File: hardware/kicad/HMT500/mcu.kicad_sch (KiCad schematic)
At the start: 7 parts, among them J2 TC2030-IDC-NL, U4 STM32G0B1CCT3

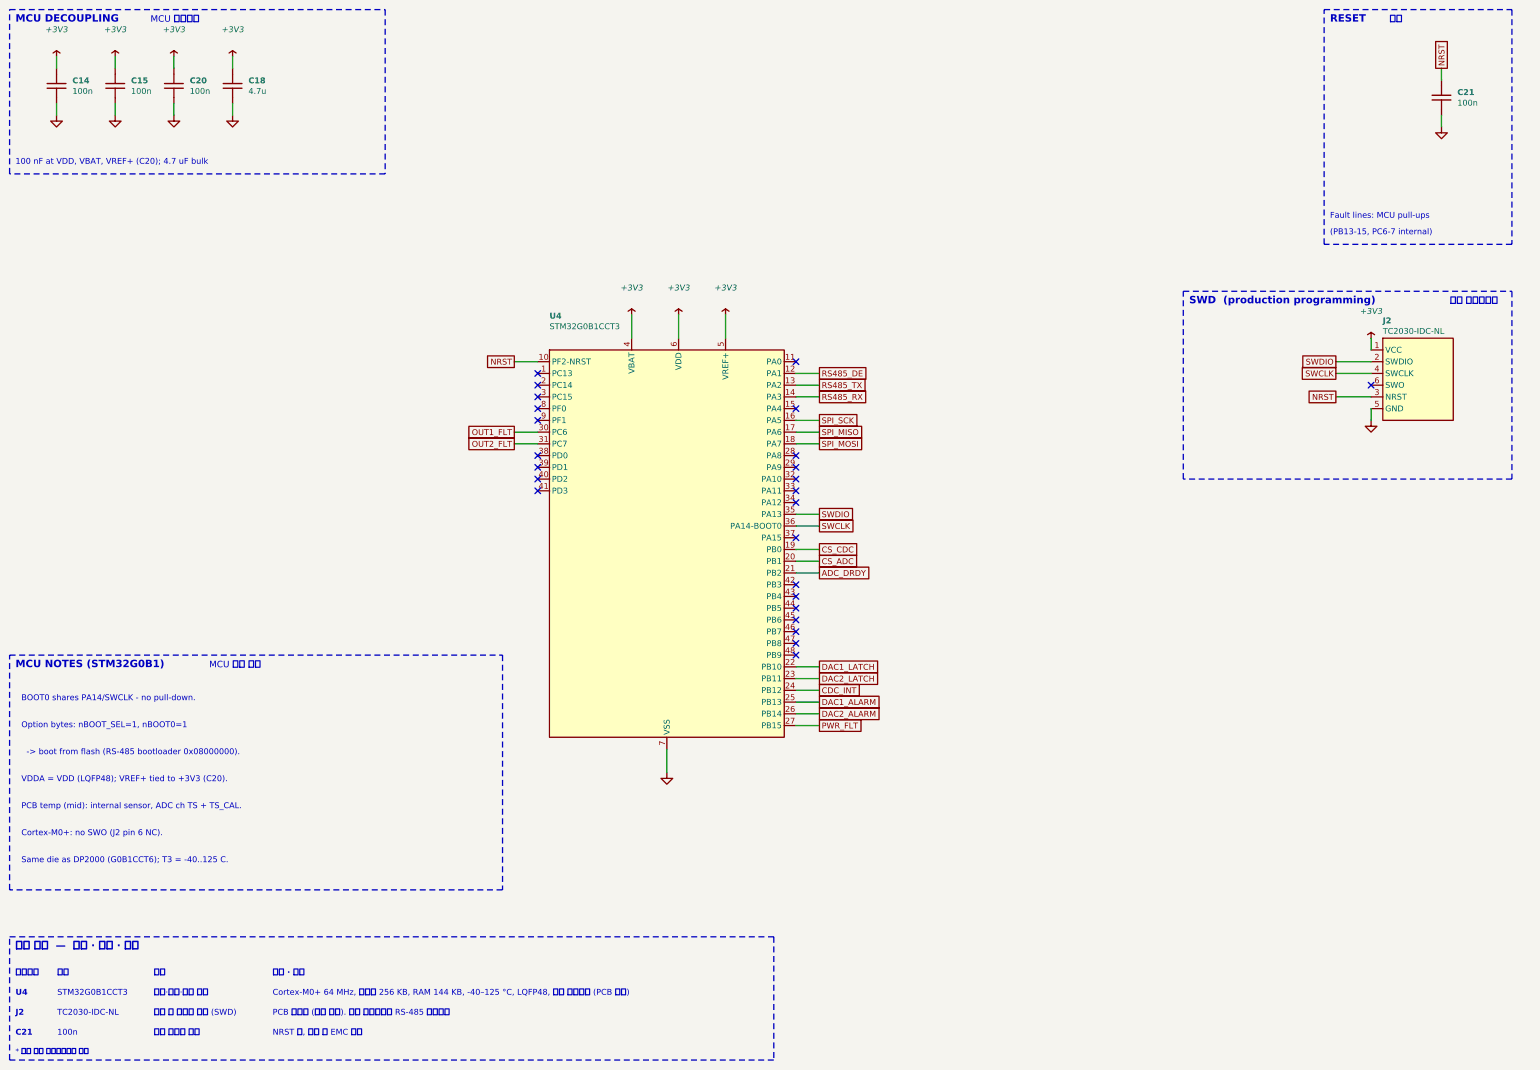
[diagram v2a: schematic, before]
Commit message: Schematic v0.7: DAC8760 real pinout, OPA197 +VSENSE buffer, ISET-R, SPI2 daisy chain
- DAC8760 symbol from datasheet SBAS528D (HTSSOP-24 PWP + EP), same as
  VibrationSensor IVS320; placeholder pins removed, VERIFY flag dropped
- +VSENSE via OPA197 unity-gain follower (U12/U13) of the terminal voltage;
  R31/R41 10k kept as buffer input protection; C45/C55 V+ bypass
- External ISET-R 15k 0.1% 25 ppm (R32/R42)
- DACs on dedicated SPI2 (PB13/14/15) daisy chain with common DAC_LATCH
  (PB10); R33 100k pull-down on DAC_DAISY; ALARM -> PB11/PB3, PWR_FLT -> PB4
- Output protection unification (TPS26611 vs passive) left on hold
- Parts list, circuit-design doc, decision log #24 updated; netlist 70/70, 0 errors

Co-Authored-By: Claude Opus 5.5 <noreply@anthropic.com>
Claude-Session: https://claude.ai/code/session_01JA2o8uJsqp9Vzsg4b665ev
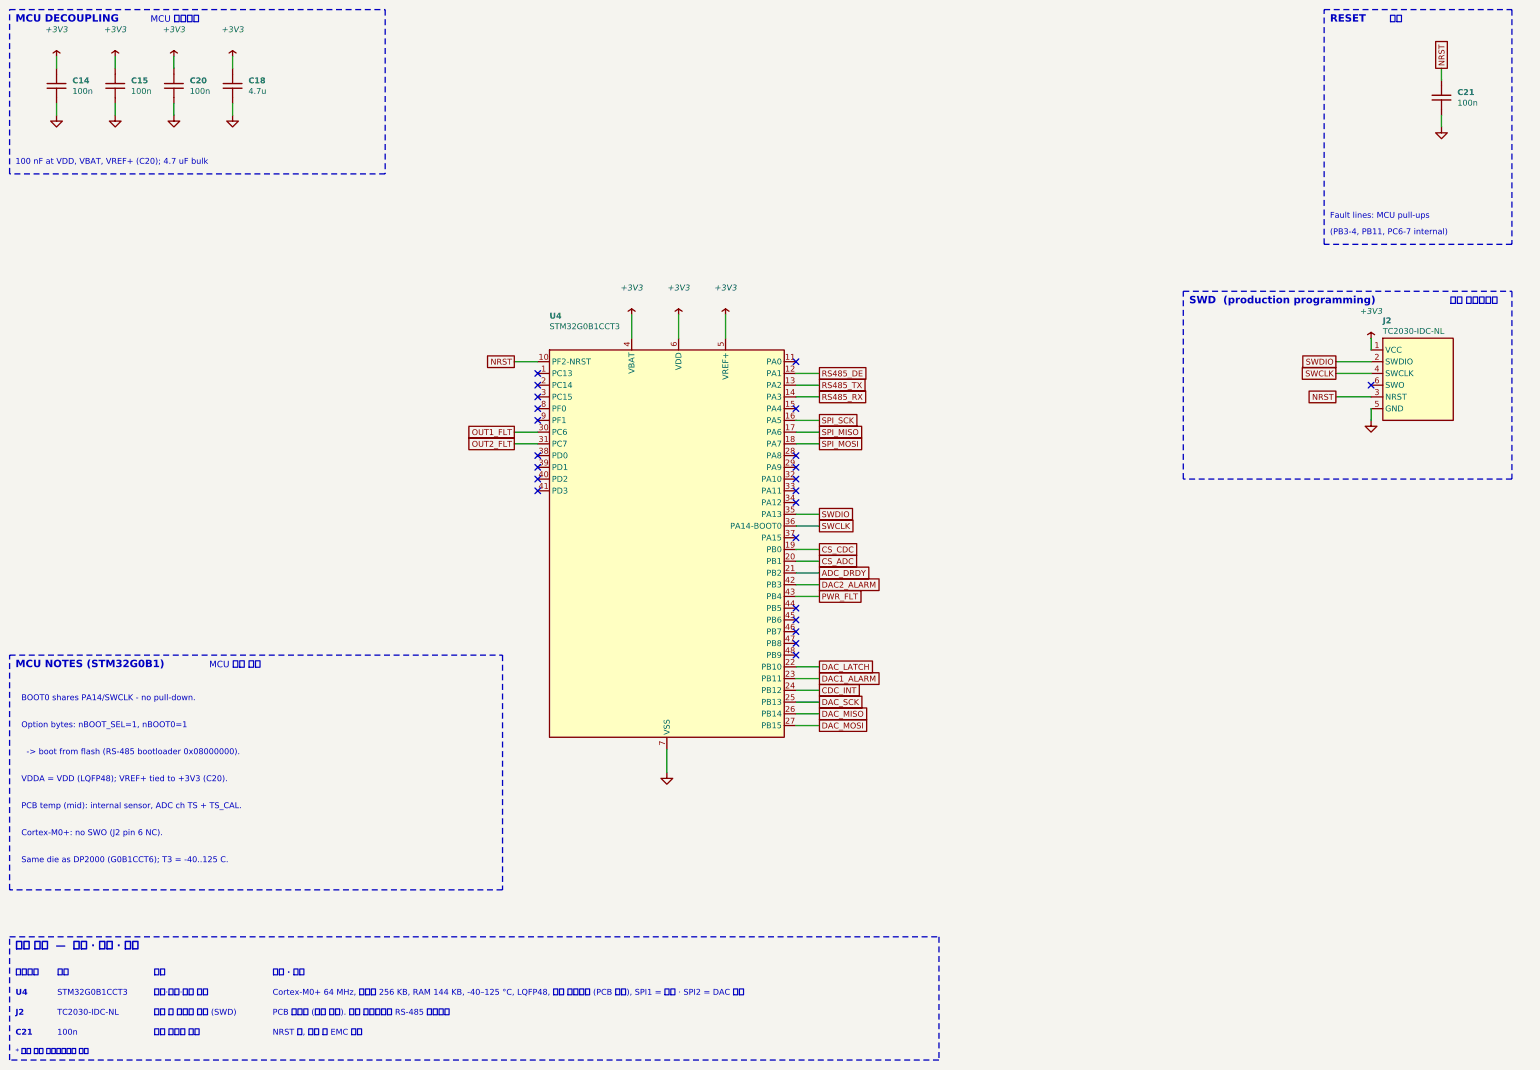
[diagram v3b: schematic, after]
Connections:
- net DAC2_LATCH is gone; now on net DAC1_ALARM: U4.23 (PB11)
- net DAC1_ALARM: no longer U4.25 (PB13)
- net DAC2_ALARM: now also U4.42 (PB3); no longer U4.26 (PB14)
- net PWR_FLT: now also U4.43 (PB4); no longer U4.27 (PB15)
- net DAC1_LATCH renamed DAC_LATCH
- new net DAC_MISO: U4.26 (PB14)
- new net DAC_MOSI: U4.27 (PB15)
- new net DAC_SCK: U4.25 (PB13)
- no-connect marks 25 -> 23
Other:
- note added: "(PB3-4, PB11, PC6-7 internal)"
- note added: "Cortex-M0+ 64 MHz, 플래시 256 KB, RAM 144 KB, -40–125 °C, LQFP48, 내부 온도센서 (PCB 온도), SPI1 = 측정 · SPI2 = DAC 전용"
- note removed: "(PB13-15, PC6-7 internal)"
- note removed: "Cortex-M0+ 64 MHz, 플래시 256 KB, RAM 144 KB, -40–125 °C, LQFP48, 내부 온도센서 (PCB 온도)"
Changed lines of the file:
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@@
 (kicad_sch (version 20230121) (generator eeschema) (paper "A3")
-(title_block (title "HMT500  MCU") (date "2026-09-29") (rev "0.6") (company "DOTECH Co., Ltd.") (comment 1 "Oil moisture transmitter HMT500 - RS-485 + 2x V/I analog output") (comment 2 "Design notes: docs/hw/circuit-design.md") (comment 3 "VERIFY=YES parts: pin numbers LMR36006/PCAP04/DAC8760/TPS26611; TPS2660 R22"))
+(title_block (title "HMT500  MCU") (date "2026-09-29") (rev "0.7") (company "DOTECH Co., Ltd.") (comment 1 "Oil moisture transmitter HMT500 - RS-485 + 2x V/I analog output") (comment 2 "Design notes: docs/hw/circuit-design.md") (comment 3 "VERIFY=YES parts: pin numbers LMR36006/PCAP04/TPS26611; TPS2660 R22"))
 (symbol (lib_id "HMT500:STM32G0B1CxTx") (at 172.72 147.32 0) (unit 1) (in_bom yes) (on_board yes) (dnp no) (property "Reference" "U4" (at 147.32 99.314 0) (effects (font (size 1.27 1.27) bold) (justify left))) (property "Value" "STM32G0B1CCT3" (at 147.32 101.6 0) (effects (font (size 1.27 1.27)) (justify left))) (property "Footprint" "Package_QFP:LQFP-48_7x7mm_P0.5mm" (at 172.72 147.32 0) (effects (font (size 1.27 1.27)) hide)) (property "Datasheet" "~" (at 172.72 147.32 0) (effects (font (size 1.27 1.27)) hide)) (pin "10") (pin "1") (pin "2") (pin "3") (pin "8") (pin "9") (pin "30") (pin "31") (pin "38") (pin "39") (pin "40") (pin "41") (pin "11") (pin "12") (pin "13") (pin "14") (pin "15") (pin "16") (pin "17") (pin "18") (pin "28") (pin "29") (pin "32") (pin "33") (pin "34") (pin "35") (pin "36") (pin "37") (pin "19") (pin "20") (pin "21") (pin "42") (pin "43") (pin "44") (pin "45") (pin "46") (pin "47") (pin "48") (pin "22") (pin "23") (pin "24") (pin "25") (pin "26") (pin "27") (pin "4") (pin "6") (pin "5") (pin "7") (instances (project "HMT500" (path "/1ebb025b-11bd-5f7c-aaab-41e2a750e8b3/0c4bf7d4-9d5c-53b1-9acd-02d419e0823f" (reference "U4") (unit 1)))))
 (symbol (lib_id "HMT500:+3V3") (at 165.1 99.06 0) (unit 1) (in_bom no) (on_board no) (dnp no) (property "Reference" "#PWR043" (at 165.1 90.932 0) (effects (font (size 1.27 1.27) bold) hide)) (property "Value" "+3V3" (at 165.1 93.218 0) (effects (font (size 1.27 1.27) italic))) (property "Footprint" "" (at 165.1 99.06 0) (effects (font (size 1.27 1.27)) hide)) (property "Datasheet" "~" (at 165.1 99.06 0) (effects (font (size 1.27 1.27)) hide)) (pin "1") (instances (project "HMT500" (path "/1ebb025b-11bd-5f7c-aaab-41e2a750e8b3/0c4bf7d4-9d5c-53b1-9acd-02d419e0823f" (reference "#PWR043") (unit 1)))))
@@
 (wire (pts (xy 200.66 152.4) (xy 205.74 152.4)) (stroke (width 0) (type default)))
 (wire (pts (xy 200.66 154.94) (xy 205.74 154.94)) (stroke (width 0) (type default)))
+(wire (pts (xy 200.66 157.48) (xy 205.74 157.48)) (stroke (width 0) (type default)))
+(wire (pts (xy 200.66 160.02) (xy 205.74 160.02)) (stroke (width 0) (type default)))
 (wire (pts (xy 200.66 175.26) (xy 205.74 175.26)) (stroke (width 0) (type default)))
 (wire (pts (xy 200.66 177.8) (xy 205.74 177.8)) (stroke (width 0) (type default)))
@@
 (global_label "CS_ADC" (shape passive) (at 205.74 152.4 0) (fields_autoplaced) (effects (font (size 1.27 1.27)) (justify left)) (property "Intersheetrefs" "${INTERSHEET_REFS}" (at 205.74 152.4 0) (effects (font (size 1.27 1.27)) hide)))
 (global_label "ADC_DRDY" (shape passive) (at 205.74 154.94 0) (fields_autoplaced) (effects (font (size 1.27 1.27)) (justify left)) (property "Intersheetrefs" "${INTERSHEET_REFS}" (at 205.74 154.94 0) (effects (font (size 1.27 1.27)) hide)))
-(global_label "DAC1_LATCH" (shape passive) (at 205.74 175.26 0) (fields_autoplaced) (effects (font (size 1.27 1.27)) (justify left)) (property "Intersheetrefs" "${INTERSHEET_REFS}" (at 205.74 175.26 0) (effects (font (size 1.27 1.27)) hide)))
-(global_label "DAC2_LATCH" (shape passive) (at 205.74 177.8 0) (fields_autoplaced) (effects (font (size 1.27 1.27)) (justify left)) (property "Intersheetrefs" "${INTERSHEET_REFS}" (at 205.74 177.8 0) (effects (font (size 1.27 1.27)) hide)))
+(global_label "DAC2_ALARM" (shape passive) (at 205.74 157.48 0) (fields_autoplaced) (effects (font (size 1.27 1.27)) (justify left)) (property "Intersheetrefs" "${INTERSHEET_REFS}" (at 205.74 157.48 0) (effects (font (size 1.27 1.27)) hide)))
+(global_label "PWR_FLT" (shape passive) (at 205.74 160.02 0) (fields_autoplaced) (effects (font (size 1.27 1.27)) (justify left)) (property "Intersheetrefs" "${INTERSHEET_REFS}" (at 205.74 160.02 0) (effects (font (size 1.27 1.27)) hide)))
+(global_label "DAC_LATCH" (shape passive) (at 205.74 175.26 0) (fields_autoplaced) (effects (font (size 1.27 1.27)) (justify left)) (property "Intersheetrefs" "${INTERSHEET_REFS}" (at 205.74 175.26 0) (effects (font (size 1.27 1.27)) hide)))
+(global_label "DAC1_ALARM" (shape passive) (at 205.74 177.8 0) (fields_autoplaced) (effects (font (size 1.27 1.27)) (justify left)) (property "Intersheetrefs" "${INTERSHEET_REFS}" (at 205.74 177.8 0) (effects (font (size 1.27 1.27)) hide)))
 (global_label "CDC_INT" (shape passive) (at 205.74 180.34 0) (fields_autoplaced) (effects (font (size 1.27 1.27)) (justify left)) (property "Intersheetrefs" "${INTERSHEET_REFS}" (at 205.74 180.34 0) (effects (font (size 1.27 1.27)) hide)))
-(global_label "DAC1_ALARM" (shape passive) (at 205.74 182.88 0) (fields_autoplaced) (effects (font (size 1.27 1.27)) (justify left)) (property "Intersheetrefs" "${INTERSHEET_REFS}" (at 205.74 182.88 0) (effects (font (size 1.27 1.27)) hide)))
-(global_label "DAC2_ALARM" (shape passive) (at 205.74 185.42 0) (fields_autoplaced) (effects (font (size 1.27 1.27)) (justify left)) (property "Intersheetrefs" "${INTERSHEET_REFS}" (at 205.74 185.42 0) (effects (font (size 1.27 1.27)) hide)))
-(global_label "PWR_FLT" (shape passive) (at 205.74 187.96 0) (fields_autoplaced) (effects (font (size 1.27 1.27)) (justify left)) (property "Intersheetrefs" "${INTERSHEET_REFS}" (at 205.74 187.96 0) (effects (font (size 1.27 1.27)) hide)))
+(global_label "DAC_SCK" (shape passive) (at 205.74 182.88 0) (fields_autoplaced) (effects (font (size 1.27 1.27)) (justify left)) (property "Intersheetrefs" "${INTERSHEET_REFS}" (at 205.74 182.88 0) (effects (font (size 1.27 1.27)) hide)))
+(global_label "DAC_MISO" (shape passive) (at 205.74 185.42 0) (fields_autoplaced) (effects (font (size 1.27 1.27)) (justify left)) (property "Intersheetrefs" "${INTERSHEET_REFS}" (at 205.74 185.42 0) (effects (font (size 1.27 1.27)) hide)))
+(global_label "DAC_MOSI" (shape passive) (at 205.74 187.96 0) (fields_autoplaced) (effects (font (size 1.27 1.27)) (justify left)) (property "Intersheetrefs" "${INTERSHEET_REFS}" (at 205.74 187.96 0) (effects (font (size 1.27 1.27)) hide)))
 (global_label "NRST" (shape passive) (at 340.36 45.72 90) (fields_autoplaced) (effects (font (size 1.27 1.27)) (justify left)) (property "Intersheetrefs" "${INTERSHEET_REFS}" (at 340.36 45.72 0) (effects (font (size 1.27 1.27)) hide)))
 (global_label "SWDIO" (shape passive) (at 317.5 109.22 180) (fields_autoplaced) (effects (font (size 1.27 1.27)) (justify right)) (property "Intersheetrefs" "${INTERSHEET_REFS}" (at 317.5 109.22 0) (effects (font (size 1.27 1.27)) hide)))
@@
 (no_connect (at 200.66 139.7))
 (no_connect (at 200.66 147.32))
-(no_connect (at 200.66 157.48))
-(no_connect (at 200.66 160.02))
 (no_connect (at 200.66 162.56))
 (no_connect (at 200.66 165.1))
@@
 (rectangle (start 284.48 93.98) (end 355.6 134.62) (stroke (width 0.1524) (type dash) (color 72 72 160 1)) (fill (type none)))
 (rectangle (start 30.48 172.72) (end 137.16 223.52) (stroke (width 0.1524) (type dash) (color 72 72 160 1)) (fill (type none)))
-(rectangle (start 30.48 233.68) (end 195.859 260.35) (stroke (width 0.1524) (type dash) (color 72 72 160 1)) (fill (type none)))
+(rectangle (start 30.48 233.68) (end 231.61 260.35) (stroke (width 0.1524) (type dash) (color 72 72 160 1)) (fill (type none)))
 (text "MCU DECOUPLING" (at 31.75 36.068 0) (effects (font (size 1.6 1.6) bold) (justify left bottom)))
 (text "MCU 바이패스" (at 60.9616 36.068 0) (effects (font (face "NanumGothic") (size 1.4 1.4)) (justify left bottom)))
@@
 (text "리셋" (at 329.112 36.068 0) (effects (font (face "NanumGothic") (size 1.4 1.4)) (justify left bottom)))
 (text "Fault lines: MCU pull-ups" (at 316.23 78.486 0) (effects (font (size 1.27 1.27)) (justify left bottom)))
-(text "(PB13-15, PC6-7 internal)" (at 316.23 82.042 0) (effects (font (size 1.27 1.27)) (justify left bottom)))
+(text "(PB3-4, PB11, PC6-7 internal)" (at 316.23 82.042 0) (effects (font (size 1.27 1.27)) (justify left bottom)))
 (text "SWD  (production programming)" (at 285.75 97.028 0) (effects (font (size 1.6 1.6) bold) (justify left bottom)))
 (text "생산 프로그래밍" (at 342.178 97.028 0) (effects (font (face "NanumGothic") (size 1.4 1.4)) (justify left bottom)))
@@
 (text "STM32G0B1CCT3" (at 40.7924 246.634 0) (effects (font (size 1.27 1.27)) (justify left bottom)))
 (text "제어·통신·보정 연산" (at 61.6839 246.634 0) (effects (font (face "NanumGothic") (size 1.27 1.27)) (justify left bottom)))
-(text "Cortex-M0+ 64 MHz, 플래시 256 KB, RAM 144 KB, -40–125 °C, LQFP48, 내부 온도센서 (PCB 온도)" (at 87.4014 246.634 0) (effects (font (face "NanumGothic") (size 1.27 1.27)) (justify left bottom)))
+(text "Cortex-M0+ 64 MHz, 플래시 256 KB, RAM 144 KB, -40–125 °C, LQFP48, 내부 온도센서 (PCB 온도), SPI1 = 측정 · SPI2 = DAC 전용" (at 87.4014 246.634 0) (effects (font (face "NanumGothic") (size 1.27 1.27)) (justify left bottom)))
 (text "J2" (at 31.75 250.952 0) (effects (font (size 1.27 1.27) bold) (justify left bottom)))
 (text "TC2030-IDC-NL" (at 40.7924 250.952 0) (effects (font (size 1.27 1.27)) (justify left bottom)))
